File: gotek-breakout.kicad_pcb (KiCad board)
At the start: 2 copper layers, 101.6 x 76.5 mm, 14 parts, among them J1 FFC 10x1 0.5mm, J10 FFC 10x1 0.5mm, J11 USB Breakout, J12 USB Micro, J2 USB_A, J3 OLED, J4 Encoder, J7 J7 Right Angle Connector, J8 J8 Mirror

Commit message: Adds notes
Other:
- board text added: "GOTEK ARTERY OLED/ROTARY BREAKOUT UNDERLINED CONNECTIONS REQUIRED"
- board text added: "J7 CONNECTS VIA RIGHT-ANGLE 2X2 J8 USE DUPONT JUMPERS J11 SOLDER TO UNDERSIDE OF USB-A OR RIGHT SIDE OF R1,R2 OR PLUG USB MICRO"
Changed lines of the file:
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@@
+		(layer "F.SilkS")
+	)
+	(gr_line
+		(start 54.8 100.7)
+		(end 57.2 100.7)
+		(stroke
+			(width 0.15)
+			(type default)
+		)
+		(layer "F.SilkS")
+	)
+	(gr_line
+		(start 61 100.7)
+		(end 62.4 100.7)
+		(stroke
+			(width 0.15)
+			(type default)
+		)
+		(layer "F.SilkS")
+	)
+	(gr_line
+		(start 54.8 103.3)
+		(end 57.2 103.3)
+		(stroke
+			(width 0.15)
+			(type default)
+		)
+		(layer "F.SilkS")
+	)
+	(gr_line
+		(start 81.2 106.1)
+		(end 82.8 106.1)
+		(stroke
+			(width 0.15)
+			(type default)
+		)
+		(layer "F.SilkS")
+	)
+	(gr_line
+		(start 45.9 100.7)
+		(end 48.1 100.7)
+		(stroke
+			(width 0.15)
+			(type default)
+		)
 		(layer "F.SilkS")
 	)
@@
 		)
 		(fill none)
+		(layer "F.SilkS")
+	)
+	(gr_line
+		(start 81.2 103.4)
+		(end 82.8 103.4)
+		(stroke
+			(width 0.15)
+			(type default)
+		)
+		(layer "F.SilkS")
+	)
+	(gr_line
+		(start 69.6 105.9)
+		(end 71.5 105.9)
+		(stroke
+			(width 0.15)
+			(type default)
+		)
+		(layer "F.SilkS")
+	)
+	(gr_line
+		(start 69.5 103.3)
+		(end 71.5 103.3)
+		(stroke
+			(width 0.15)
+			(type default)
+		)
+		(layer "F.SilkS")
+	)
+	(gr_line
+		(start 61.2 103.3)
+		(end 62.3 103.3)
+		(stroke
+			(width 0.15)
+			(type default)
+		)
 		(layer "F.SilkS")
 	)
@@
 		(layer "Edge.Cuts")
 	)
+	(gr_text "J7 CONNECTS VIA RIGHT-ANGLE 2X2\nJ8 USE DUPONT JUMPERS\nJ11 SOLDER TO UNDERSIDE OF USB-A\nOR RIGHT SIDE OF R1,R2\nOR PLUG USB MICRO"
+		(at 82.8 115.1 0)
+		(layer "B.SilkS")
+		(effects
+			(font
+				(size 1 1)
+				(thickness 0.15)
+			)
+			(justify left bottom mirror)
+		)
+	)
 	(gr_text "JLCJLCJLCJLC"
 		(at 58.3 115.5 0)
@@
 		)
 	)
+	(gr_text "GOTEK ARTERY OLED/ROTARY BREAKOUT\nUNDERLINED CONNECTIONS REQUIRED"
+		(at 46 111.9 0)
+		(layer "F.SilkS")
+		(effects
+			(font
+				(size 0.8 0.8)
+				(thickness 0.15)
+			)
+			(justify left bottom)
+		)
+	)

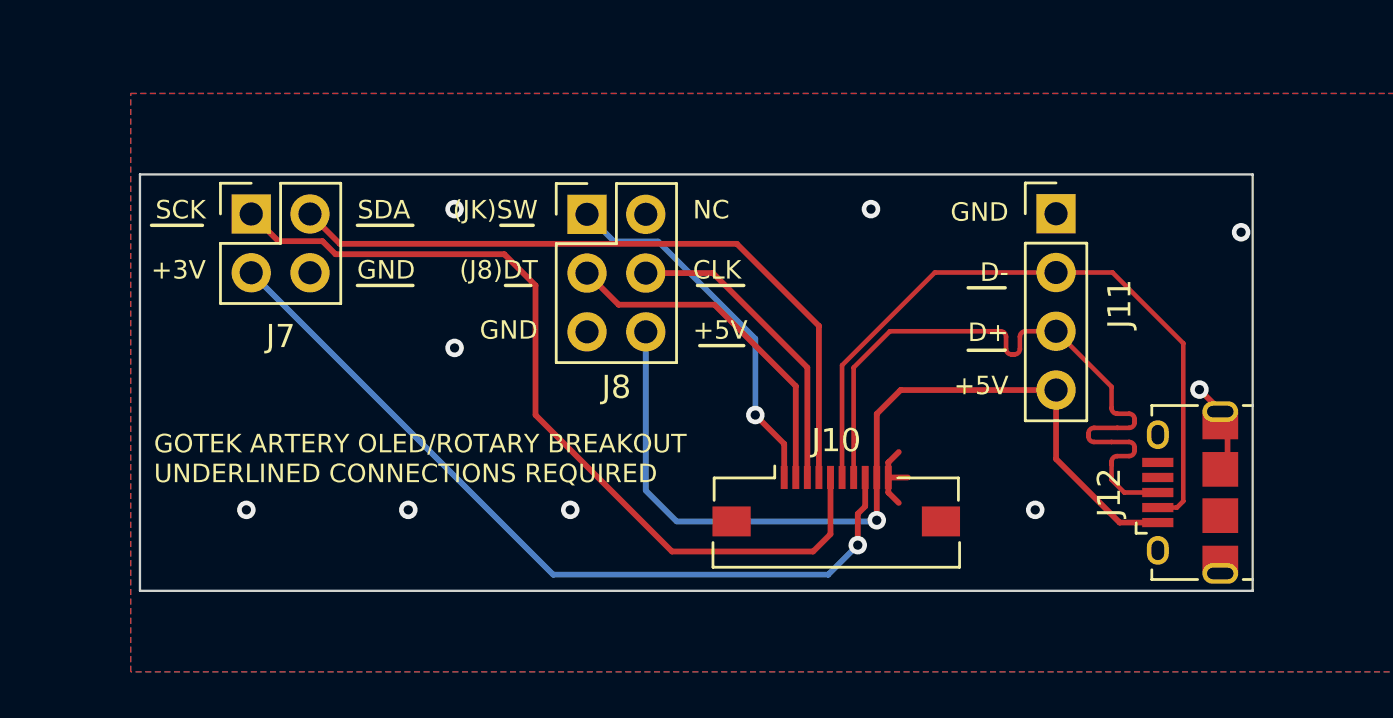
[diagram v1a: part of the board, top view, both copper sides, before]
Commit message: Match D+/D- positions better
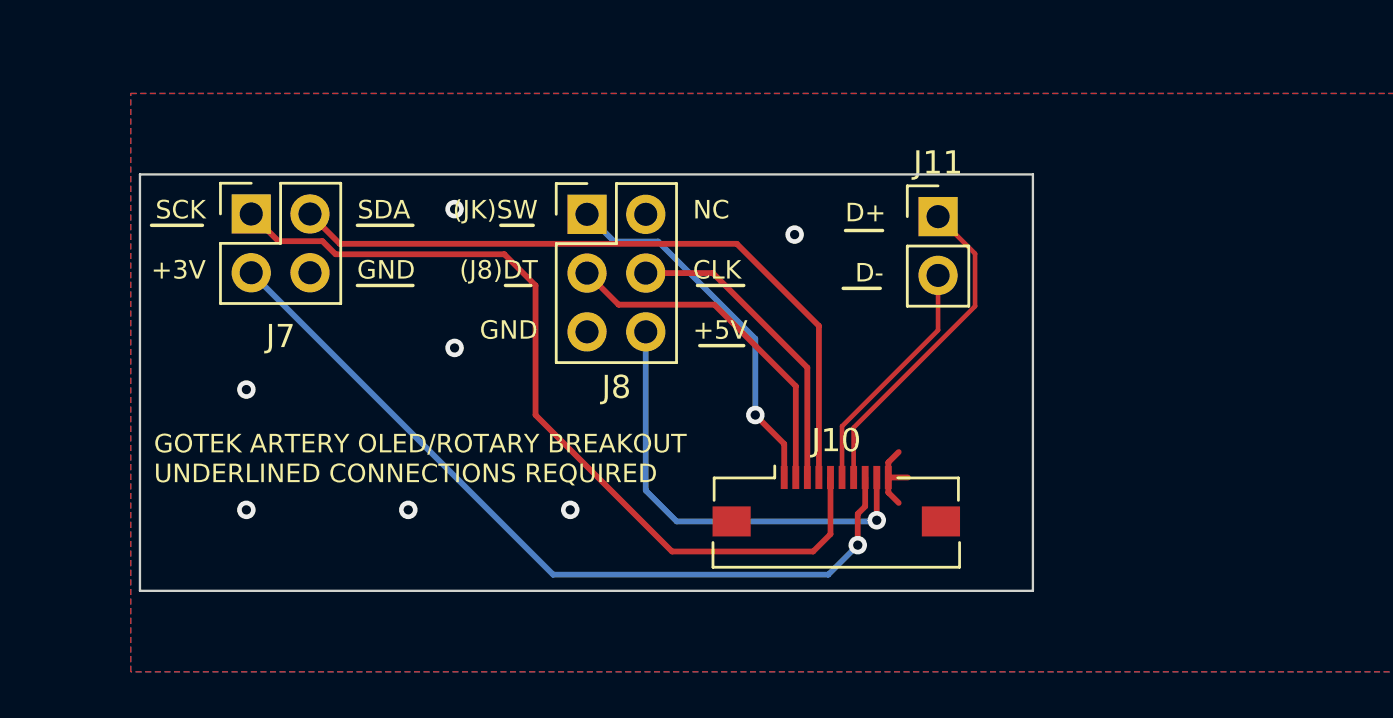
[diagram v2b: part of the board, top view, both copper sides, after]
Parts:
- removed J12: USB Micro, Connector_USB:USB_Micro-B_Amphenol_10118194_Horizontal
- J11: footprint Connector_PinHeader_2.54mm:PinHeader_1x04_P2.54mm_Vertical -> Connector_PinHeader_2.54mm:PinHeader_1x02_P2.54mm_Vertical
- moved J11 5.10 mm to (79.9, 100.3)
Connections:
- J11 pad 1: /Gotek Side/GND -> /Gotek Side/USB_D+
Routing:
- net /Gotek Side/USB_D-: track 30.6 -> 10.5 mm
- net /Gotek Side/+5V: track 38.7 -> 19.3 mm
- net /Gotek Side/USB_D+: track 30.4 -> 14.1 mm
- net /Gotek Side/GND: track 7.08 -> 3.42 mm, vias 9 -> 7
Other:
- outline, holes or cut-outs redrawn

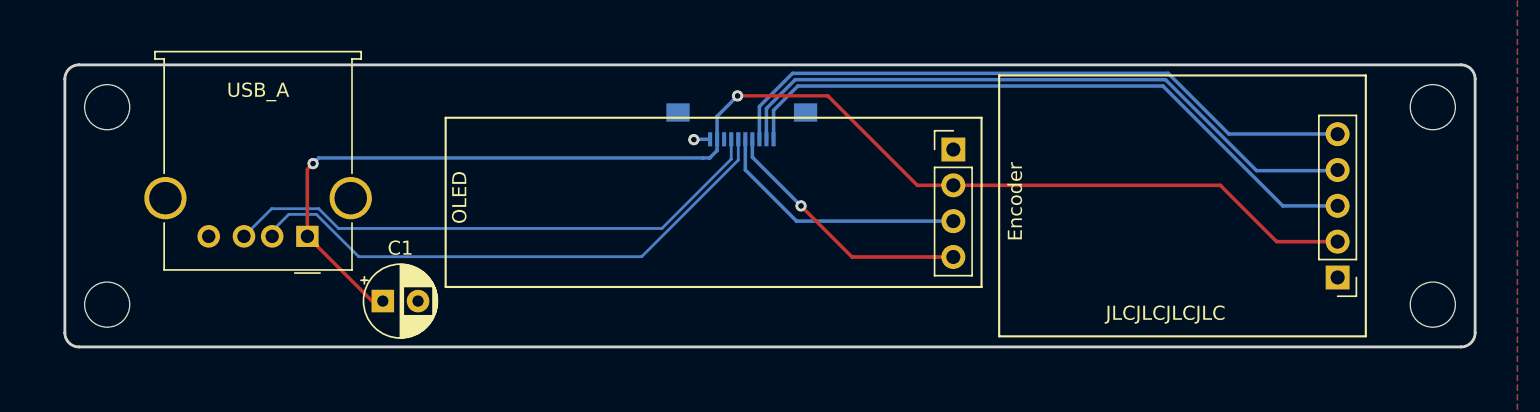
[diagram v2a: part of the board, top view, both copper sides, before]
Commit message: M2 mounting holes to match 3d print
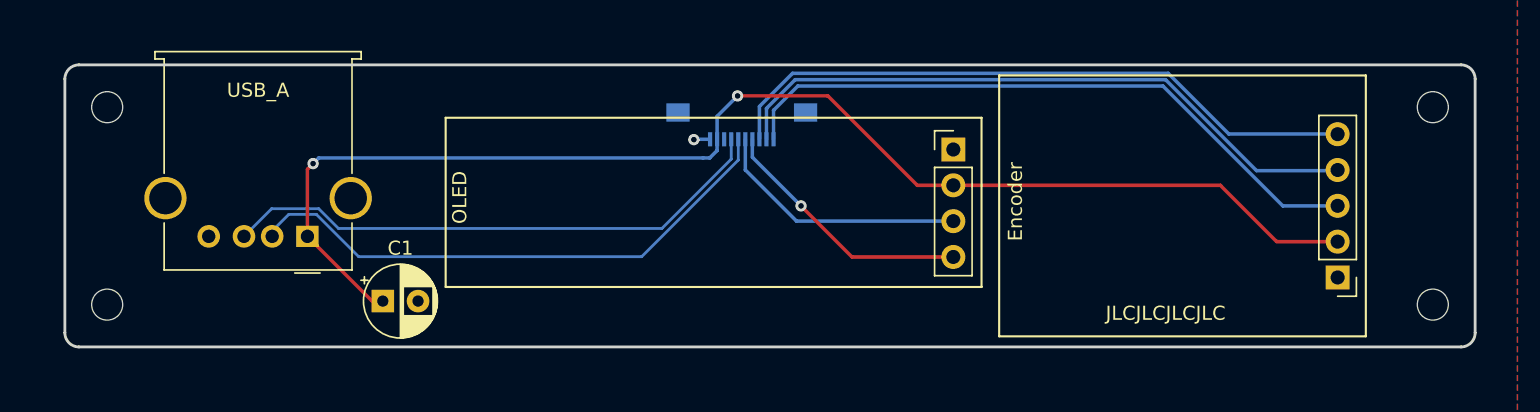
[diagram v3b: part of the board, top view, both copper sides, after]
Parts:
- H1, H2, H3, H4: value MountingHole_3.2mm_M3 -> MountingHole_2.2mm_M2; footprint MountingHole:MountingHole_3.2mm_M3 -> MountingHole:MountingHole_2.2mm_M2
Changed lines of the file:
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@@
 		)
 	)
-	(footprint "MountingHole:MountingHole_3.2mm_M3"
+	(footprint "MountingHole:MountingHole_2.2mm_M2"
 		(layer "F.Cu")
 		(at 50 43)
-		(descr "Mounting Hole 3.2mm, no annular, M3")
-		(tags "mounting hole 3.2mm no annular m3")
+		(descr "Mounting Hole 2.2mm, no annular, M2")
+		(tags "mounting hole 2.2mm no annular m2")
 		(property "Reference" "H1"
 			(at 0 -4.2 0)
@@
 			)
 		)
-		(property "Value" "MountingHole_3.2mm_M3"
+		(property "Value" "MountingHole_2.2mm_M2"
 			(at 0 4.2 0)
 			(layer "F.Fab")
@@
 			)
 		)
-		(clearance 1)
 		(attr board_only exclude_from_pos_files exclude_from_bom)
 		(fp_circle
 			(center 0 0)
-			(end 3.2 0)
+			(end 2.2 0)
 			(stroke
 				(width 0.15)
@@
 		(fp_circle
 			(center 0 0)
-			(end 3.45 0)
+			(end 2.45 0)
 			(stroke
 				(width 0.05)
@@
 		(pad "" np_thru_hole circle
 			(at 0 0)
-			(size 3.2 3.2)
-			(drill 3.2)
+			(size 2.2 2.2)
+			(drill 2.2)
 			(layers "*.Cu" "*.Mask")
 		)
@@
 		(tags "Through hole pin header THT 1x02 2.54mm single row")
 		(property "Reference" "J11"
-			(at 0 -2.33 360)
+			(at 0 -2.33 0)
 			(layer "F.SilkS")
 			(effects
@@
 		)
 		(property "Value" "USB Breakout"
-			(at 0 4.87 360)
+			(at 0 4.87 0)
 			(layer "F.Fab")
 			(effects
@@
 		)
 	)
-	(footprint "MountingHole:MountingHole_3.2mm_M3"
+	(footprint "MountingHole:MountingHole_2.2mm_M2"
 		(layer "F.Cu")
 		(at 144 57)
-		(descr "Mounting Hole 3.2mm, no annular, M3")
-		(tags "mounting hole 3.2mm no annular m3")
+		(descr "Mounting Hole 2.2mm, no annular, M2")
+		(tags "mounting hole 2.2mm no annular m2")
 		(property "Reference" "H4"
 			(at 0 -4.2 0)
@@
 			)
 		)
-		(property "Value" "MountingHole_3.2mm_M3"
+		(property "Value" "MountingHole_2.2mm_M2"
 			(at 0 4.2 0)
 			(layer "F.Fab")
@@
 			)
 		)
-		(clearance 1)
 		(attr board_only exclude_from_pos_files exclude_from_bom)
 		(fp_circle
 			(center 0 0)
-			(end 3.2 0)
+			(end 2.2 0)
 			(stroke
 				(width 0.15)
@@
 		(fp_circle
 			(center 0 0)
-			(end 3.45 0)
+			(end 2.45 0)
 			(stroke
 				(width 0.05)
@@
 		(pad "" np_thru_hole circle
 			(at 0 0)
-			(size 3.2 3.2)
-			(drill 3.2)
-			(layers "F&B.Cu" "*.Mask")
+			(size 2.2 2.2)
+			(drill 2.2)
+			(layers "*.Cu" "*.Mask")
 		)
 	)
@@
 		)
 	)
-	(footprint "MountingHole:MountingHole_3.2mm_M3"
+	(footprint "MountingHole:MountingHole_2.2mm_M2"
 		(layer "F.Cu")
 		(at 144 43)
-		(descr "Mounting Hole 3.2mm, no annular, M3")
-		(tags "mounting hole 3.2mm no annular m3")
+		(descr "Mounting Hole 2.2mm, no annular, M2")
+		(tags "mounting hole 2.2mm no annular m2")
 		(property "Reference" "H3"
 			(at 0 -4.2 0)
@@
 			)
 		)
-		(property "Value" "MountingHole_3.2mm_M3"
+		(property "Value" "MountingHole_2.2mm_M2"
 			(at 0 4.2 0)
 			(layer "F.Fab")
@@
 			)
 		)
-		(clearance 1)
 		(attr board_only exclude_from_pos_files exclude_from_bom)
 		(fp_circle
 			(center 0 0)
-			(end 3.2 0)
+			(end 2.2 0)
 			(stroke
 				(width 0.15)
@@
 		(fp_circle
 			(center 0 0)
-			(end 3.45 0)
+			(end 2.45 0)
 			(stroke
 				(width 0.05)
@@
 		(pad "" np_thru_hole circle
 			(at 0 0)
-			(size 3.2 3.2)
-			(drill 3.2)
+			(size 2.2 2.2)
+			(drill 2.2)
 			(layers "*.Cu" "*.Mask")
 		)
 	)
-	(footprint "MountingHole:MountingHole_3.2mm_M3"
+	(footprint "MountingHole:MountingHole_2.2mm_M2"
 		(layer "F.Cu")
 		(at 50 57)
-		(descr "Mounting Hole 3.2mm, no annular, M3")
-		(tags "mounting hole 3.2mm no annular m3")
+		(descr "Mounting Hole 2.2mm, no annular, M2")
+		(tags "mounting hole 2.2mm no annular m2")
 		(property "Reference" "H2"
 			(at 0 -4.2 0)
@@
 			)
 		)
-		(property "Value" "MountingHole_3.2mm_M3"
+		(property "Value" "MountingHole_2.2mm_M2"
 			(at 0 4.2 0)
 			(layer "F.Fab")
@@
 			)
 		)
-		(clearance 1)
 		(attr board_only exclude_from_pos_files exclude_from_bom)
 		(fp_circle
 			(center 0 0)
-			(end 3.2 0)
+			(end 2.2 0)
 			(stroke
 				(width 0.15)
@@
 		(fp_circle
 			(center 0 0)
-			(end 3.45 0)
+			(end 2.45 0)
 			(stroke
 				(width 0.05)
@@
 		(pad "" np_thru_hole circle
 			(at 0 0)
-			(size 3.2 3.2)
-			(drill 3.2)
-			(layers "F&B.Cu" "*.Mask")
+			(size 2.2 2.2)
+			(drill 2.2)
+			(layers "*.Cu" "*.Mask")
 		)
 	)
